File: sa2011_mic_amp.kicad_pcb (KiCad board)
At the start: 2 copper layers, 32.8 x 35.8 mm, 16 parts, among them J2 Conn_01x02_Pin, SW1 SW_SPST, U1 SA2011

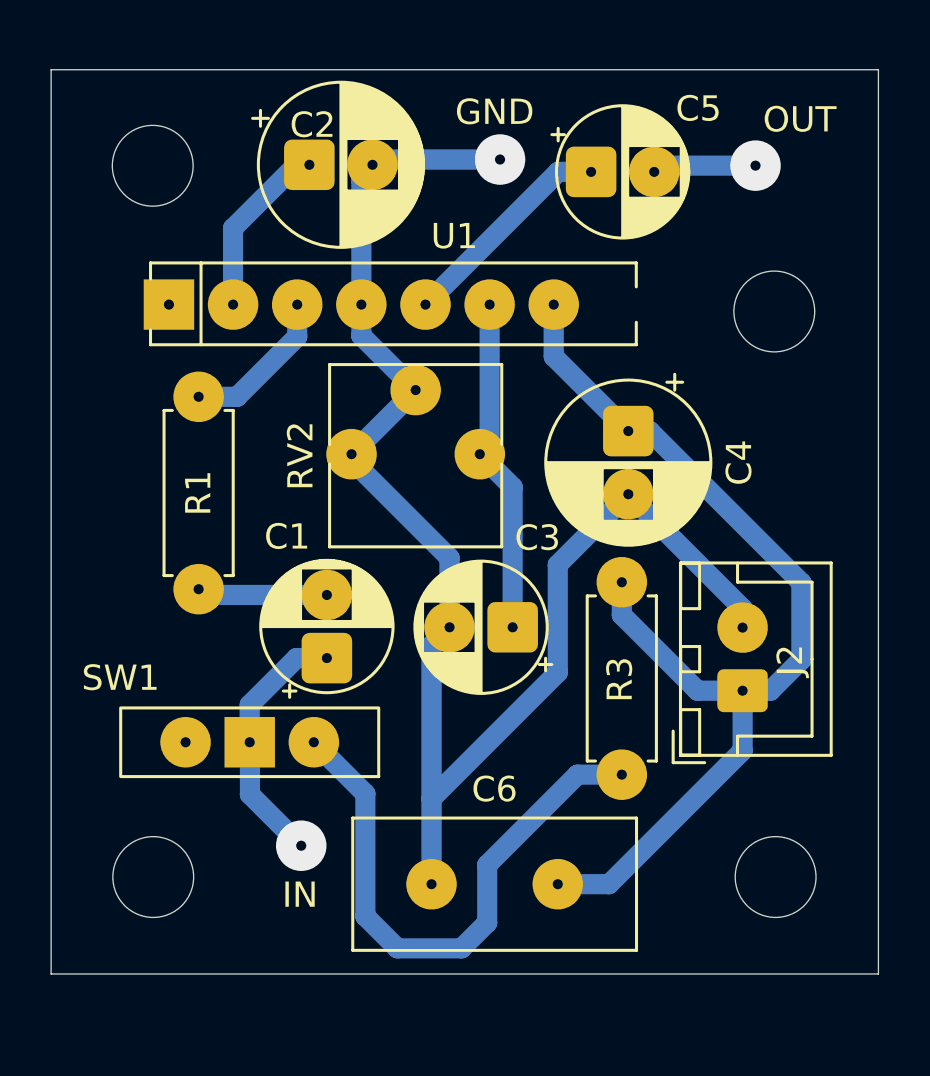
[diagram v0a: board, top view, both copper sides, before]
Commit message: 縦長に配置を変更
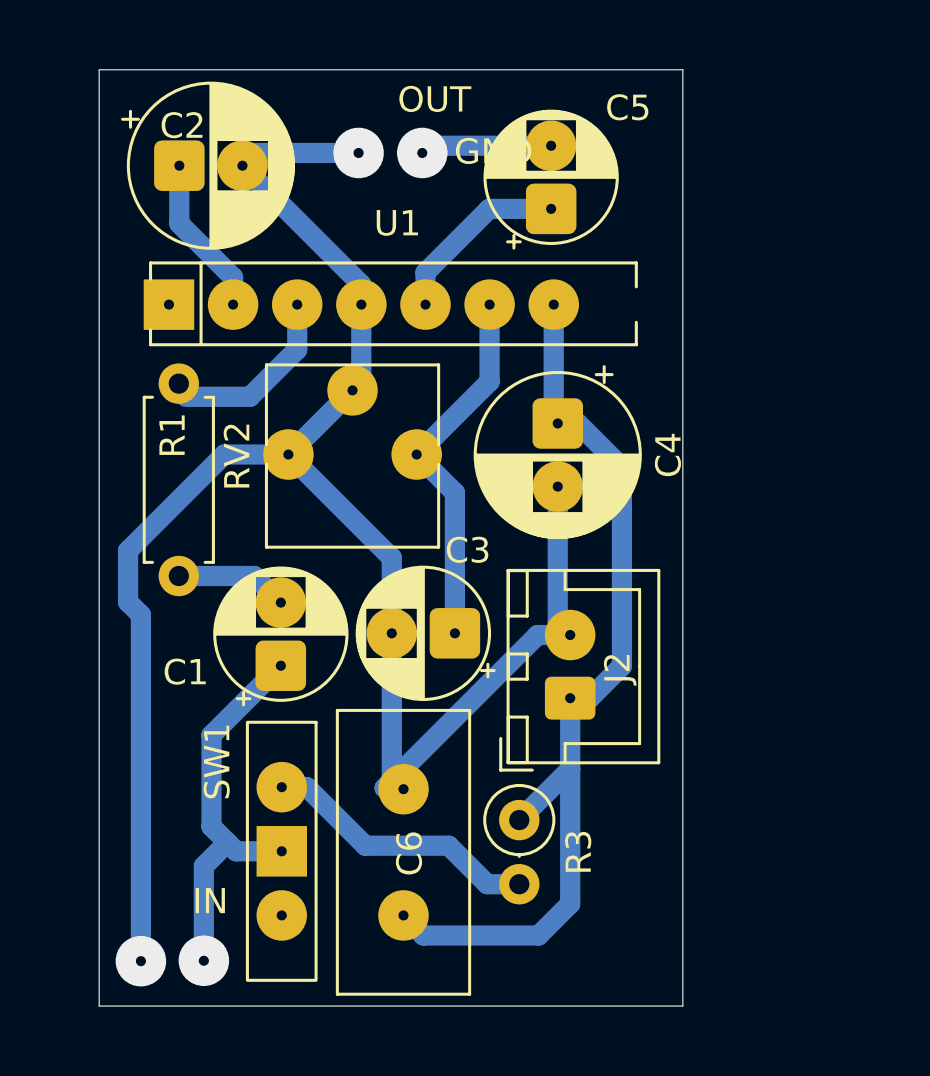
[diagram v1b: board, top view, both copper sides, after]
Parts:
- removed H1, H2, H3, H4: MountingHole, MountingHole:MountingHole_3.2mm_M3
- R3: footprint Resistor_THT:R_Axial_DIN0207_L6.3mm_D2.5mm_P7.62mm_Horizontal -> Resistor_THT:R_Axial_DIN0207_L6.3mm_D2.5mm_P2.54mm_Vertical
- moved R3 10.3 mm to (160.8, 94.2)
- moved J2 6.83 mm to (162.8, 89.4)
- moved C2 5.15 mm to (147.3, 68.3)
- moved SW1 4.50 mm to (151.4, 95.5), turned to -90 degrees
- moved C6 3.92 mm to (156.2, 93.0), turned to -90 degrees
- moved C4 2.81 mm to (162.3, 78.5)
- moved RV2 2.50 mm to (156.7, 79.8)
- moved C3 2.30 mm to (158.2, 86.8)
- moved C5 2.16 mm to (162.0, 70.0), turned to 90 degrees
- moved C1 1.85 mm to (151.3, 88.1)
- moved R1 0.94 mm to (147.3, 76.9)
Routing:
- net GND: track 60.0 -> 75.0 mm, vias 1 -> 2
- net Net-(SW1-B): track 22.6 -> 11.0 mm
- net Net-(SW1-A): track 10.5 -> 16.0 mm
- net VCC 4～14v: track 40.7 -> 36.9 mm
- net Net-(U1-OUT): track 8.74 -> 7.29 mm
- net Net-(U1-DETOUT): track 13.5 -> 14.8 mm
- net Net-(C5-Pad2): track 4.06 -> 5.22 mm
- net Net-(U1-IN): track 6.16 -> 6.97 mm
- net Net-(U1-IN-): track 7.09 -> 6.38 mm
- net Net-(C1-Pad2): track 5.17 -> 4.48 mm
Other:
- board size 32.8 x 35.8 mm -> 23.1 x 37.1 mm

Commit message: パッド修正、ベタ追加
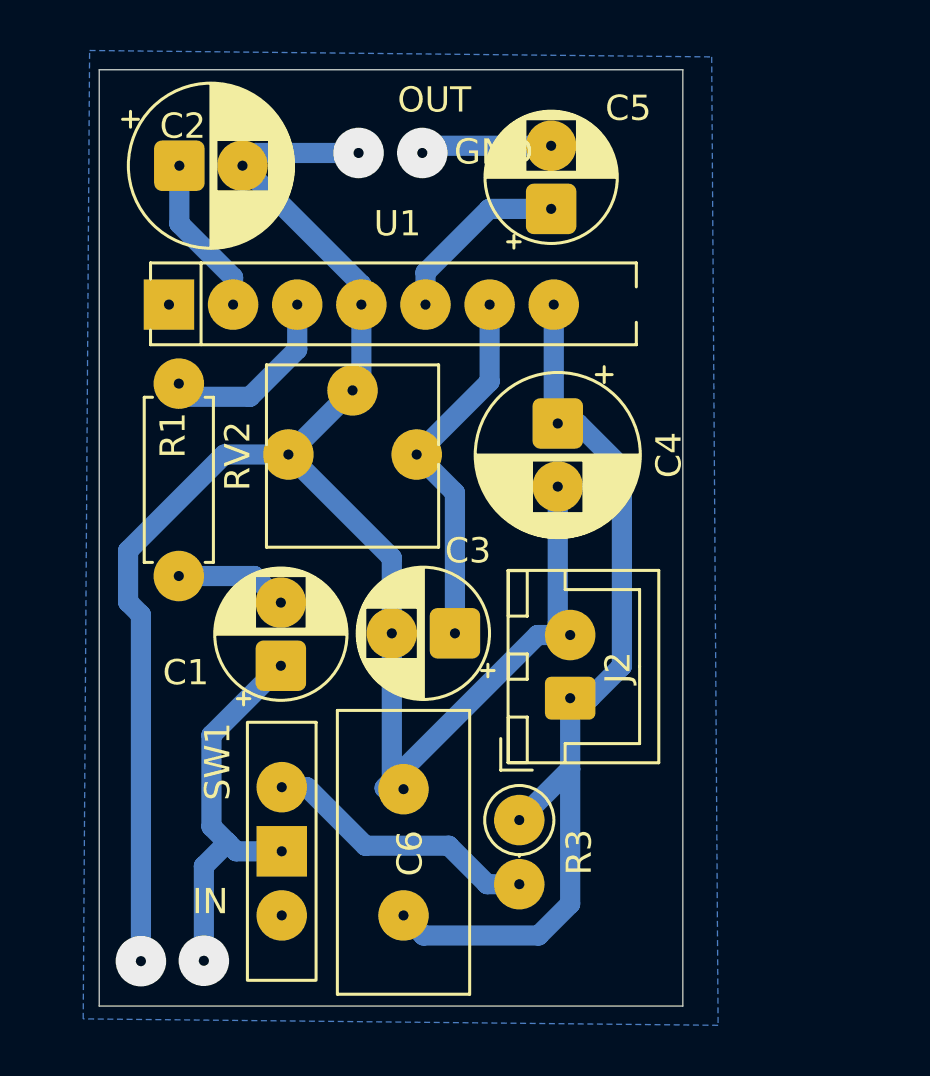
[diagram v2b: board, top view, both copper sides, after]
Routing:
- added copper zone on B.Cu, net (none)
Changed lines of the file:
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@@
 		(pad "1" thru_hole circle
 			(at 0 0 270)
-			(size 1.6 1.6)
-			(drill 0.8)
+			(size 2 2)
+			(drill 0.4)
 			(layers "*.Cu" "*.Mask")
 			(remove_unused_layers no)
@@
 		(pad "2" thru_hole circle
 			(at 7.62 0 270)
-			(size 1.6 1.6)
-			(drill 0.8)
+			(size 2 2)
+			(drill 0.4)
 			(layers "*.Cu" "*.Mask")
 			(remove_unused_layers no)
@@
 		(pad "1" thru_hole circle
 			(at 0 0 270)
-			(size 1.6 1.6)
-			(drill 0.8)
+			(size 2 2)
+			(drill 0.4)
 			(layers "*.Cu" "*.Mask")
 			(remove_unused_layers no)
@@
 		(pad "2" thru_hole circle
 			(at 2.54 0 270)
-			(size 1.6 1.6)
-			(drill 0.8)
+			(size 2 2)
+			(drill 0.4)
 			(layers "*.Cu" "*.Mask")
 			(remove_unused_layers no)
@@
 		(net 11)
 	)
+	(zone
+		(net 0)
+		(net_name "")
+		(layer "B.Cu")
+		(hatch edge 0.5)
+		(connect_pads
+			(clearance 0.5)
+		)
+		(min_thickness 0.25)
+		(filled_areas_thickness no)
+		(fill yes
+			(thermal_gap 0.5)
+			(thermal_bridge_width 0.5)
+			(island_removal_mode 1)
+			(island_area_min 10)
+		)
+		(polygon
+			(pts
+				(xy 143.764 63.754) (xy 168.402 64.008) (xy 168.656 102.362) (xy 143.51 102.108)
+			)
+		)
+	)
 	(embedded_fonts no)
